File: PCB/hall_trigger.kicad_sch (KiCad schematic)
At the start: 2 parts

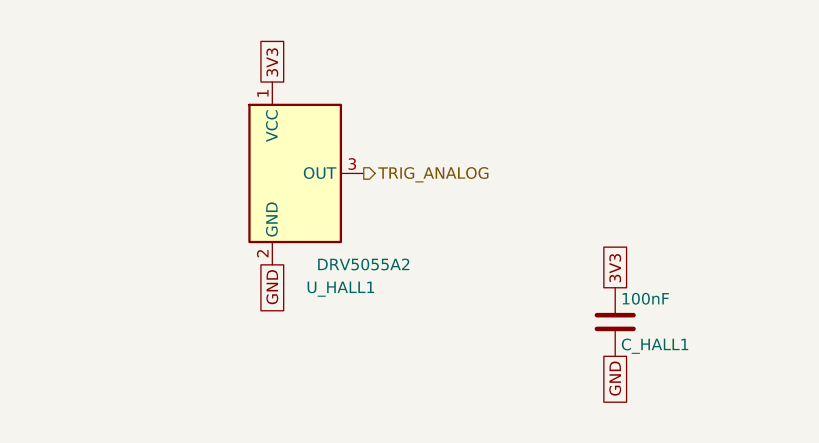
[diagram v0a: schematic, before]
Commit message: refactor: updated gulikit footprint
This updates the gulikit thumbstick footprint to be accurate.
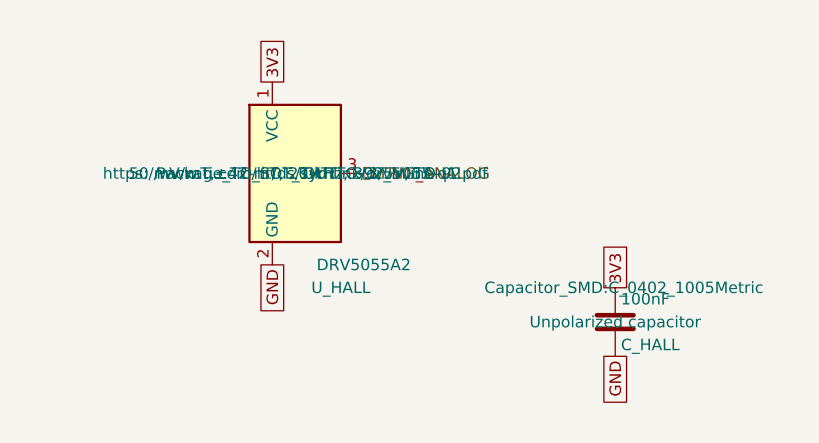
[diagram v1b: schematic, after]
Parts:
- removed C_HALL1: 100nF, Capacitor_SMD:C_0402_1005Metric, symbol Device:C
- removed U_HALL1: DRV5055A2, Package_TO_SOT_THT:TO-92_Inline, symbol Sensor_Magnetic:DRV5055A2xLPGxQ1
- added C_HALL: 100nF, Capacitor_SMD:C_0402_1005Metric, symbol Device:C
- added U_HALL: DRV5055A2, Package_TO_SOT_THT:TO-92_Inline, symbol Sensor_Magnetic:DRV5055A2xLPGxQ1
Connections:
- net 3V3: now also C_HALL.1, U_HALL.1 (VCC)
- net GND: now also C_HALL.2, U_HALL.2 (GND)
- net TRIG_ANALOG: now also U_HALL.3 (OUT)
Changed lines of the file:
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@@
 	(generator_version "10.0")
 	(paper "A4")
+	(global_label "3V3"
+		(shape passive)
+		(at 166.37 109.22 90)
+		(fields_autoplaced yes)
+		(effects
+			(font
+				(size 1.27 1.27)
+			)
+			(justify left)
+		)
+		(property "Intersheetrefs" "${INTERSHEET_REFS}"
+			(at 166.37 109.22 0)
+			(hide yes)
+			(show_name no)
+			(do_not_autoplace no)
+			(effects
+				(font
+					(size 1.27 1.27)
+				)
+			)
+		)
+	)
 	(global_label "GND"
 		(shape passive)
+		(at 128.27 106.68 270)
+		(fields_autoplaced yes)
+		(effects
+			(font
+				(size 1.27 1.27)
+			)
+			(justify right)
+		)
+		(property "Intersheetrefs" "${INTERSHEET_REFS}"
+			(at 128.27 106.68 0)
+			(hide yes)
+			(show_name no)
+			(do_not_autoplace no)
+			(effects
+				(font
+					(size 1.27 1.27)
+				)
+			)
+		)
+	)
+	(global_label "GND"
+		(shape passive)
 		(at 166.37 116.84 270)
 		(fields_autoplaced yes)
@@
 		(property "Intersheetrefs" "${INTERSHEET_REFS}"
 			(at 166.37 116.84 0)
-			(hide yes)
-			(show_name no)
-			(do_not_autoplace no)
-			(effects
-				(font
-					(size 1.27 1.27)
-				)
-			)
-		)
-	)
-	(global_label "3V3"
-		(shape passive)
-		(at 166.37 109.22 90)
-		(fields_autoplaced yes)
-		(effects
-			(font
-				(size 1.27 1.27)
-			)
-			(justify left)
-		)
-		(property "Intersheetrefs" "${INTERSHEET_REFS}"
-			(at 166.37 109.22 0)
-			(hide yes)
-			(show_name no)
-			(do_not_autoplace no)
-			(effects
-				(font
-					(size 1.27 1.27)
-				)
-			)
-		)
-	)
-	(global_label "GND"
-		(shape passive)
-		(at 128.27 106.68 270)
-		(fields_autoplaced yes)
-		(effects
-			(font
-				(size 1.27 1.27)
-			)
-			(justify right)
-		)
-		(property "Intersheetrefs" "${INTERSHEET_REFS}"
-			(at 128.27 106.68 0)
 			(hide yes)
 			(show_name no)
@@
 		(dnp no)
 		(fields_autoplaced yes)
-		(property "Reference" "C_HALL1"
+		(property "Reference" "C_HALL"
 			(at 167.005 115.57 0)
 			(show_name no)
@@
 		(property "Footprint" "Capacitor_SMD:C_0402_1005Metric"
 			(at 167.3352 109.22 0)
-			(hide yes)
 			(show_name no)
 			(do_not_autoplace no)
@@
 		(property "Datasheet" ""
 			(at 166.37 113.03 0)
-			(hide yes)
 			(show_name no)
 			(do_not_autoplace no)
@@
 		(property "Description" "Unpolarized capacitor"
 			(at 166.37 113.03 0)
-			(hide yes)
 			(show_name no)
 			(do_not_autoplace no)
@@
 		)
 		(instances
-			(project "snips_controller"
-				(path "/868f8289-8434-4465-b2f4-2accc5e40bab/3b2478ec-2890-4ec8-b56f-d58b64ce58ab"
-					(reference "C_HALL1")
+			(project ""
+				(path "/d0f5b7d7-b2b6-4492-958c-e60265d3c6b4/58aa3fea-7023-42af-afb1-45eaa756099e"
+					(reference "C_HALL")
 					(unit 1)
 				)
@@
 		(dnp no)
 		(fields_autoplaced yes)
-		(property "Reference" "U_HALL1"
+		(property "Reference" "U_HALL"
 			(at 135.89 109.22 0)
 			(show_name no)
@@
 		(property "Footprint" "Package_TO_SOT_THT:TO-92_Inline"
 			(at 130.81 96.52 0)
-			(hide yes)
 			(show_name no)
 			(do_not_autoplace no)
@@
 		(property "Datasheet" "https://www.ti.com/lit/ds/symlink/drv5055-q1.pdf"
 			(at 130.81 96.52 0)
-			(hide yes)
 			(show_name no)
 			(do_not_autoplace no)
@@
 		(property "Description" "50 mV/mT,±42-mT, 20-kHz, 3.3/5V, TO-92"
 			(at 130.81 96.52 0)
-			(hide yes)
 			(show_name no)
 			(do_not_autoplace no)
@@
 		)
 		(instances
-			(project "snips_controller"
-				(path "/868f8289-8434-4465-b2f4-2accc5e40bab/3b2478ec-2890-4ec8-b56f-d58b64ce58ab"
-					(reference "U_HALL1")
+			(project ""
+				(path "/d0f5b7d7-b2b6-4492-958c-e60265d3c6b4/58aa3fea-7023-42af-afb1-45eaa756099e"
+					(reference "U_HALL")
 					(unit 1)
 				)

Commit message: layout: beginning pcb layout
This updates the schematic with a few different footprints while also starts the layout.
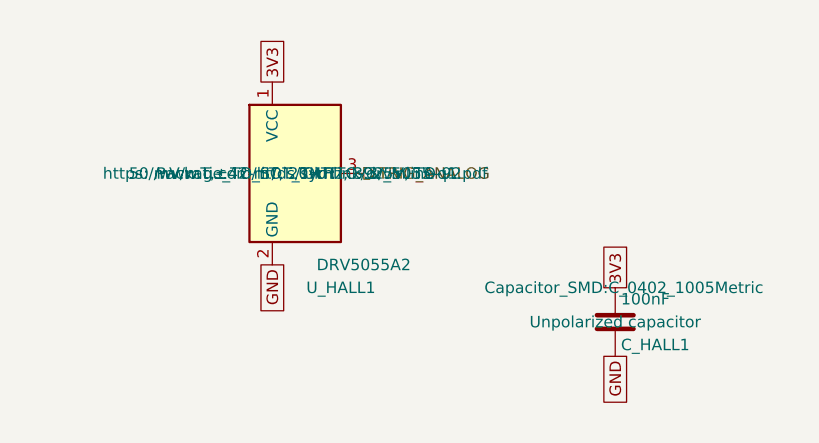
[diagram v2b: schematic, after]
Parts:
- renumbered C_HALL to C_HALL1, U_HALL to U_HALL1
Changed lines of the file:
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@@
 		(dnp no)
 		(fields_autoplaced yes)
-		(property "Reference" "C_HALL"
+		(property "Reference" "C_HALL1"
 			(at 167.005 115.57 0)
 			(show_name no)
@@
 		)
 		(instances
+			(project "snips_controller"
+				(path "/868f8289-8434-4465-b2f4-2accc5e40bab/58aa3fea-7023-42af-afb1-45eaa756099e"
+					(reference "C_HALL1")
+					(unit 1)
+				)
+			)
 			(project ""
 				(path "/d0f5b7d7-b2b6-4492-958c-e60265d3c6b4/58aa3fea-7023-42af-afb1-45eaa756099e"
@@
 		(dnp no)
 		(fields_autoplaced yes)
-		(property "Reference" "U_HALL"
+		(property "Reference" "U_HALL1"
 			(at 135.89 109.22 0)
 			(show_name no)
@@
 		)
 		(instances
+			(project "snips_controller"
+				(path "/868f8289-8434-4465-b2f4-2accc5e40bab/58aa3fea-7023-42af-afb1-45eaa756099e"
+					(reference "U_HALL1")
+					(unit 1)
+				)
+			)
 			(project ""
 				(path "/d0f5b7d7-b2b6-4492-958c-e60265d3c6b4/58aa3fea-7023-42af-afb1-45eaa756099e"
